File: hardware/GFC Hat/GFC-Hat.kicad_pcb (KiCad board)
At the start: 2 copper layers, 65 x 30 mm, 36 parts, among them J1 BAT, U2 CAT24C32WI-GT3, U3 BME280

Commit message: Started making some revisions to Prototype 2, cleaned up files.
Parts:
- removed I2C3: I2C0, Connector_PinHeader_2.00mm:PinHeader_1x04_P2.00mm_Vertical
- removed LED1: Status LED, LED_SMD:LED_0805_2012Metric
- removed R2: R, Resistor_SMD:R_0603_1608Metric_Pad0.98x0.95mm_HandSolder
- removed TMP1, TMP2, TMP3: 1-Wire Bus, Connector_PinHeader_2.00mm:PinHeader_1x03_P2.00mm_Vertical
- removed TP1: Test Point, TestPoint:TestPoint_Pad_D1.0mm
- removed the U2 at (62.5, 62.0)
- added 1W1: 1-Wire Bus, GFC-Hat-Footprints:JST_PH_B3B-PH-K_1x03_P2.00mm_Vertical, F.Cu at (78.2, 35.5)
- added 1W2: 1-Wire Bus, GFC-Hat-Footprints:JST_PH_B3B-PH-K_1x03_P2.00mm_Vertical, F.Cu at (78.2, 41.0)
- added C12: 0.1uF, Capacitor_SMD:C_0603_1608Metric_Pad1.08x0.95mm_HandSolder, F.Cu at (170.4, 5.73)
- added C13: 0.1uF, Capacitor_SMD:C_0603_1608Metric_Pad1.08x0.95mm_HandSolder, F.Cu at (183.4, 6.10)
- added C14: 0.1uF, Capacitor_SMD:C_0603_1608Metric_Pad1.08x0.95mm_HandSolder, F.Cu at (203.5, -13.9)
- added C18: 0.1uF, Capacitor_SMD:C_0603_1608Metric_Pad1.08x0.95mm_HandSolder, F.Cu at (107.6, 24.6)
- added U1: MAX17048G+T10, MAX17048G_T10:SON50P200X200X80-9N, F.Cu at (34.2, 42.1)
- added U3: CAT24C32WI-GT3, footprints:SOIC127P600X175-8N, B.Cu at (81.5, 26.4)
- added U4: DS18B20, Package_TO_SOT_THT:TO-92_Inline, F.Cu at (76.0, 30.7)
- C1: renamed from C2; footprint Capacitor_THT:CP_Radial_D6.3mm_P2.50mm -> Capacitor_SMD:C_Elec_6.3x7.7
- C2: renamed from C3; footprint Capacitor_SMD:C_0603_1608Metric_Pad1.08x0.95mm_HandSolder -> Capacitor_SMD:C_0805_2012Metric_Pad1.18x1.45mm_HandSolder
- C6: value 100nF -> 0.1uF
- D1: value 1N5400 -> 2A LFV; footprint Diode_THT:D_DO-15_P12.70mm_Horizontal -> Diode_SMD:D_SMA_Handsoldering
- I2C1, I2C2: footprint Connector_PinHeader_2.00mm:PinHeader_1x04_P2.00mm_Vertical -> GFC-Hat-Footprints:JST_PH_B4B-PH-K_1x04_P2.00mm_Vertical
- J1: footprint Library:OSTVN02A150 2x1 Terminal Block -> GFC-Hat-Footprints:OSTVN02A150 2x1 Terminal Block
- PI_HDR1: renamed from CPU1; value Pi Zero/Zero W -> PI Header
- SPI1, SPI2: footprint Connector_PinHeader_2.00mm:PinHeader_1x06_P2.00mm_Vertical -> GFC-Hat-Footprints:JST_PH_B6B-PH-K_1x06_P2.00mm_Vertical
- moved PR2 136.5 mm to (174.7, 8.24)
- moved C3 131.5 mm to (21.5, 38.3), turned to -90 degrees
- moved PR1 128.3 mm to (170.4, 8.24), turned to 0 degrees
- moved C9 125.5 mm to (31.1, 31.9)
- moved C5 125.0 mm to (35.4, 39.8)
- moved C7 122.6 mm to (31.1, 33.5)
- moved C2 116.5 mm to (23.6, 36.0), turned to 90 degrees
- moved C1 89.6 mm to (28.4, 39.0)
- moved R1 68.8 mm to (74.0, 38.0)
- moved U2 66.0 mm to (31.4, 29.4)
- moved G*** 40.7 mm to (113.0, 79.0)
- moved C6 39.0 mm to (174.7, 5.73)
- moved C10 34.9 mm to (179.1, 5.73)
- moved SPI1 32.9 mm to (48.5, 28.8), turned to 0 degrees
- moved SPI2 30.4 mm to (48.5, 34.7), turned to 0 degrees
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- renumbered C12 to C15, C13 to C16, C4 to C3, C5 to C4, C1 to C5, U3 to U2
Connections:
- C10 pad 1: +3V3 -> GND
- PI_HDR1 pad 16: /Status LED GPIO -> unconnected-(PI_HDR1-Pad16)
- R3 pad 2: +3V3 -> GND
- R4 pad 2: +3V3 -> GND
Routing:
- net +3V3: track 68.6 -> 0.00 mm
- net I2C0.SDA: track 29.8 -> 0.00 mm
- net I2C0.SCL: track 27.1 -> 0.00 mm
- net EEPROM.SDA: track 0.00 -> 23.7 mm
- net EEPROM.SCL: track 0.00 -> 23.6 mm
- net GND: track 17.9 -> 0.00 mm, vias 2 -> 0
- net 1-Wire: track 15.5 -> 0.00 mm
- net SPI0.MOSI: track 14.6 -> 0.00 mm
- net /VCC Polarized: track 0.00 -> 13.7 mm, vias 0 -> 2
- net SPI0.MISO: track 11.5 -> 0.00 mm
- net SPI0.SCLK: track 10.1 -> 0.00 mm
- net SPI0.CE0: track 8.82 -> 0.00 mm
- net SPI0.CE1: track 7.60 -> 0.00 mm
- net VCC: track 0.00 -> 3.93 mm
- net +5V: track 21.3 -> 18.2 mm
- removed copper zone on B.Cu, net GND
- removed copper zone on F.Cu, net GND
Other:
- outline, holes or cut-outs redrawn
- board text added: "GFC PROTOTYPE 2"
- board text removed: "GFC PROTOTYPE 1"
- board text removed: "HAT"

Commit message: GFC Prototype 2 Complete and ordered - with BOM
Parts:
- removed C16: 0.1uF, Capacitor_SMD:C_0603_1608Metric_Pad1.08x0.95mm_HandSolder
- removed the G*** at (113.0, 79.0)
- removed I2C2: I2C0, GFC-Hat-Footprints:JST_PH_B4B-PH-K_1x04_P2.00mm_Vertical
- removed SPI1, SPI2: SPI, GFC-Hat-Footprints:JST_PH_B6B-PH-K_1x06_P2.00mm_Vertical
- added C17: 0.1µF, Capacitor_SMD:C_0603_1608Metric, B.Cu at (29.7, 38.8)
- added C19: 0.1µF, Capacitor_SMD:C_0603_1608Metric, F.Cu at (68.8, 29.1)
- added G***: LOGO, footprints:logo2, F.Cu at (59.1, 43.1)
- added R2: 30kΩ, Resistor_SMD:R_0603_1608Metric, B.Cu at (29.4, 35.5)
- added R5: 7.5kΩ, Resistor_SMD:R_0603_1608Metric, B.Cu at (32.2, 38.3)
- added TP1: GND REF, TestPoint:TestPoint_Keystone_5019_Minature, B.Cu at (22.5, 42.6)
- added TP2: BAT REF, TestPoint:TestPoint_Pad_D1.5mm, F.Cu at (33.0, 40.8)
- added U5: BMI088, GFC-Footprints:PQFN50P450X300X100-16N, B.Cu at (52.5, 35.0)
- 1W1, 1W2: value 1-Wire Bus -> 1-Wire; footprint GFC-Hat-Footprints:JST_PH_B3B-PH-K_1x03_P2.00mm_Vertical -> Connector_PinHeader_1.27mm:PinHeader_1x03_P1.27mm_Vertical
- C1: value 100uF -> 100µF; moved to B.Cu
- C10, C11, C12, C14, C18, C7, C9: value 0.1uF -> 0.1µF; footprint Capacitor_SMD:C_0603_1608Metric_Pad1.08x0.95mm_HandSolder -> Capacitor_SMD:C_0603_1608Metric
- C13, C15, C3, C4, C5, C6, C8: value 0.1uF -> 0.1µF; footprint Capacitor_SMD:C_0603_1608Metric_Pad1.08x0.95mm_HandSolder -> Capacitor_SMD:C_0603_1608Metric; moved to B.Cu
- C2: value 1uF -> 1µF; footprint Capacitor_SMD:C_0805_2012Metric_Pad1.18x1.45mm_HandSolder -> Capacitor_SMD:C_0805_2012Metric; moved to B.Cu
- D1: footprint Diode_SMD:D_SMA_Handsoldering -> Diode_SMD:D_SMA
- I2C1: value I2C0 -> I²C; footprint GFC-Hat-Footprints:JST_PH_B4B-PH-K_1x04_P2.00mm_Vertical -> Connector_PinHeader_1.27mm:PinHeader_1x04_P1.27mm_Vertical
- J1: footprint GFC-Hat-Footprints:OSTVN02A150 2x1 Terminal Block -> GFC-Footprints:OSTVN02A150 2x1 Terminal Block
- PI_HDR1: value PI Header -> PI
- PR1, PR2: value * -> Pull-up
- R1: value 4.7k -> 4.7kΩ; footprint Resistor_SMD:R_0603_1608Metric_Pad0.98x0.95mm_HandSolder -> Resistor_SMD:R_0603_1608Metric
- R3, R4: value 3.9K -> 3.9kΩ; footprint Resistor_SMD:R_0603_1608Metric_Pad0.98x0.95mm_HandSolder -> Resistor_SMD:R_0603_1608Metric
- U1: value MAX17048G+T10 -> MCP3021; footprint MAX17048G_T10:SON50P200X200X80-9N -> Package_TO_SOT_SMD:SOT-23-5; moved to B.Cu
- U3: value CAT24C32WI-GT3 -> CAT24C32
- U4: value DS18B20 -> SAM-M8Q; footprint Package_TO_SOT_THT:TO-92_Inline -> RF_GPS:ublox_SAM-M8Q
- VR1: moved to F.Cu
- moved C14 177.7 mm to (36.0, 45.7)
- moved C6 150.5 mm to (25.1, 21.5), turned to 180 degrees
- moved C12 146.3 mm to (29.7, 45.7)
- moved PR2 141.7 mm to (37.0, 41.6), turned to -90 degrees
- moved C13 137.4 mm to (49.0, 34.5)
- moved PR1 136.0 mm to (38.5, 41.6), turned to -90 degrees
- moved C4 120.3 mm to (25.6, 27.4), turned to -90 degrees
- moved C10 109.3 mm to (72.3, 29.1), turned to 180 degrees
- moved C11 105.9 mm to (40.8, 45.7)
- moved C15 97.6 mm to (55.3, 36.3), turned to 90 degrees
- moved R4 69.6 mm to (79.4, 24.6), turned to -90 degrees
- moved C8 62.8 mm to (82.5, 21.5)
- moved R3 61.9 mm to (81.0, 24.6), turned to -90 degrees
- moved 1W1 51.9 mm to (27.9, 48.2), turned to 90 degrees
- moved 1W2 44.6 mm to (34.2, 48.2), turned to 90 degrees
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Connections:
- net /VCC Polarized renamed BAT_P
- C10 pad 2: GND -> +3V3
- C18 pad 1: +3V3 -> GND
- C18 pad 2: GND -> +3V3
- C5 pad 1: VCC -> GND
- C5 pad 2: GND -> +3V3
- D1 pad 2: VCC -> +BATT
- I2C1 pad 2: I2C0.SCL -> +3V3
- I2C1 pad 4: +3V3 -> I2C0.SCL
- J1 pad 1: VCC -> +BATT
- PI_HDR1 pad 13: unconnected-(PI_HDR1-Pad13) -> BMI088 Int1
- PI_HDR1 pad 15: unconnected-(PI_HDR1-Pad15) -> BMI088 Int3
- PI_HDR1 pad 37: unconnected-(PI_HDR1-Pad37) -> TX_Ready GPIO
- R3 pad 2: GND -> +3V3
- R4 pad 2: GND -> +3V3
- U1 pad 1: GND -> +3V3
- U1 pad 2: VCC -> GND
- U1 pad 3: +3V3 -> /BAT Reference
- U1 pad 4: GND -> I2C0.SDA
- U1 pad 5: unconnected-(U1-Pad5) -> I2C0.SCL
- U4 pad 2: 1-Wire -> +3V3
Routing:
- net I2C0.SDA: track 0.00 -> 71.0 mm, vias 0 -> 3
- net I2C0.SCL: track 0.00 -> 67.6 mm, vias 0 -> 2
- net GND: track 0.00 -> 48.1 mm, vias 0 -> 59
- net +3V3: track 0.00 -> 46.9 mm, vias 0 -> 19
- net TX_Ready GPIO: track 0.00 -> 41.8 mm, vias 0 -> 1
- net 1-Wire: track 0.00 -> 38.8 mm, vias 0 -> 1
- net BMI088 Int1: track 0.00 -> 21.4 mm
- net SPI0.CE0: track 0.00 -> 18.0 mm
- net SPI0.CE1: track 0.00 -> 17.0 mm
- net BMI088 Int3: track 0.00 -> 16.2 mm, vias 0 -> 2
- net SPI0.MISO: track 0.00 -> 14.7 mm, vias 0 -> 2
- net SPI0.SCLK: track 0.00 -> 11.1 mm
- net /BAT Reference: track 0.00 -> 10.5 mm, vias 0 -> 1
- net SPI0.MOSI: track 0.00 -> 8.73 mm
- net VCC: track 3.93 -> 0.00 mm
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- added copper zone on In2.Cu, net +3V3
- added copper zone on B.Cu, net GND
- added copper zone on F.Cu, net GND
- added copper zone on In1.Cu, net GND
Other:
- outline, holes or cut-outs redrawn
- copper layers 2 -> 4
- board text added: "IMU"

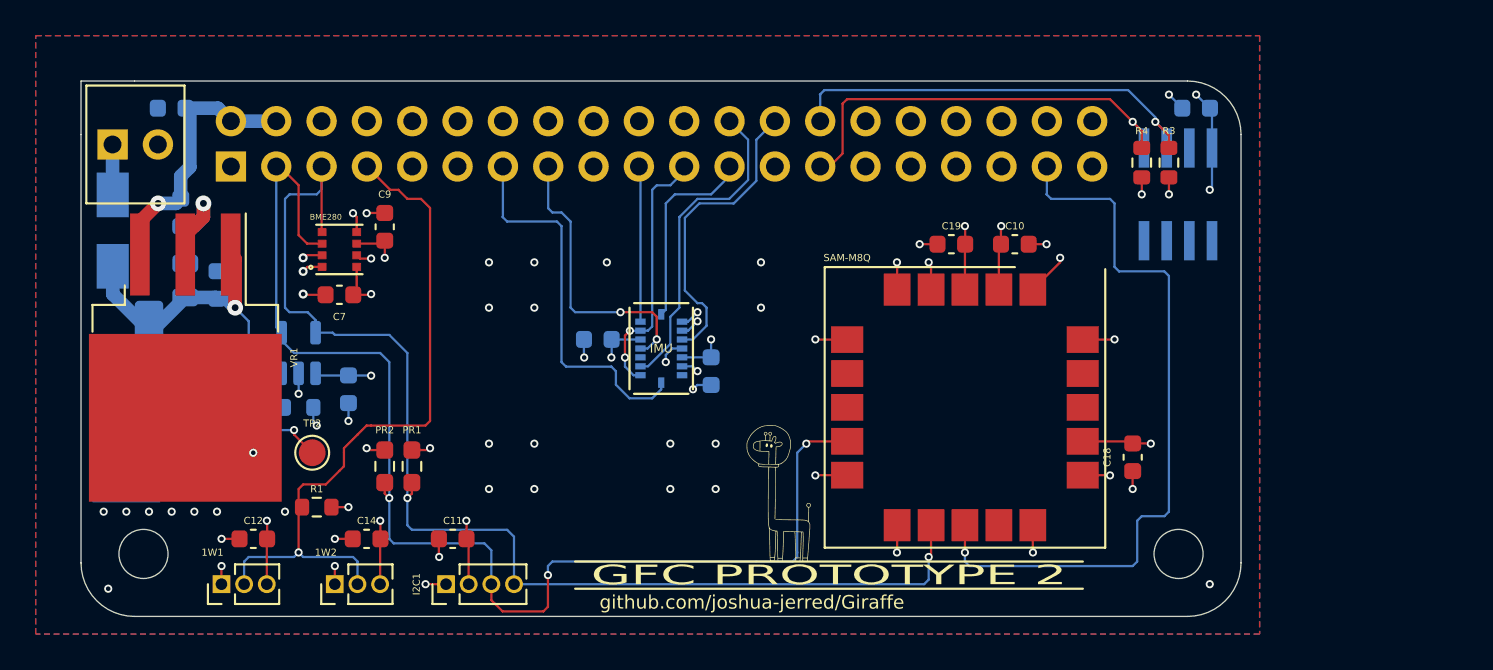
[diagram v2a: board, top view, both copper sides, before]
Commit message: Hardware update to bring it up to KiCad 7.0
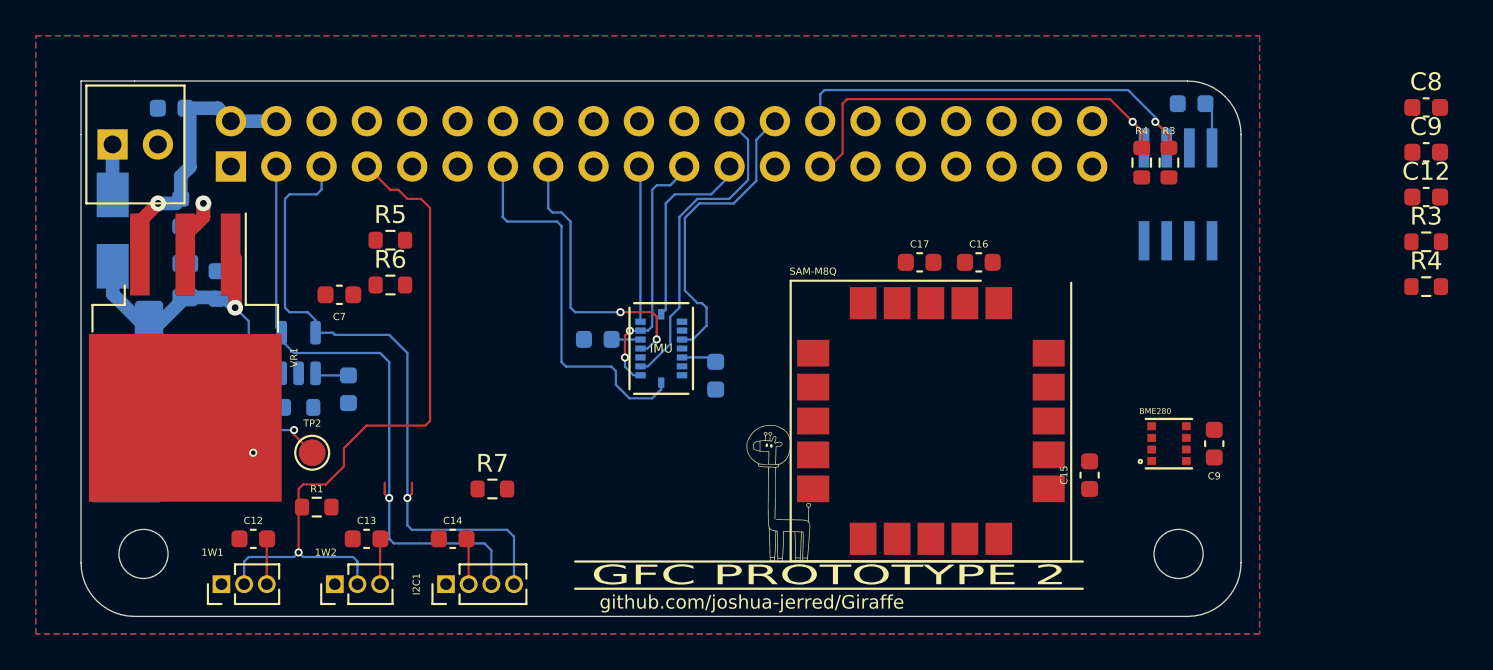
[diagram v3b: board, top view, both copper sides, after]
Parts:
- removed PR1, PR2: Pull-up, Resistor_SMD:R_0603_1608Metric_Pad0.98x0.95mm_HandSolder
- added C12: 0.1µF, Capacitor_SMD:C_0603_1608Metric, F.Cu at (95.4, 26.5)
- added C8: 0.1µF, Capacitor_SMD:C_0603_1608Metric, F.Cu at (95.4, 21.5)
- added C9: 0.1µF, Capacitor_SMD:C_0603_1608Metric, F.Cu at (95.4, 24.0)
- added R3: 3.9kΩ, Resistor_SMD:R_0603_1608Metric, F.Cu at (95.4, 29.0)
- added R4: 3.9kΩ, Resistor_SMD:R_0603_1608Metric, F.Cu at (95.4, 31.5)
- added R5: *, Resistor_SMD:R_0603_1608Metric, F.Cu at (37.3, 28.9)
- added R6: *, Resistor_SMD:R_0603_1608Metric, F.Cu at (37.3, 31.4)
- added R7: 4.7kΩ, Resistor_SMD:R_0603_1608Metric, F.Cu at (43.0, 42.9)
- R1: value 4.7kΩ -> 30kΩ
- U3: footprint footprints:SOIC127P600X175-8N -> GFC-Footprints:SOIC127P600X175-8N
- moved C9 48.0 mm to (83.5, 40.3), turned to -90 degrees
- moved U2 47.7 mm to (81.0, 40.3)
- moved C15 2.61 mm to (76.5, 42.1)
- moved C16 2.26 mm to (70.3, 30.2)
- moved U4 2.05 mm to (67.6, 39.0)
- moved C17 2.05 mm to (67.0, 30.2)
- moved C18 0.36 mm to (55.6, 36.5)
- moved C10 0.36 mm to (82.2, 21.3)
- renumbered C8 to C10, C13 to C11, C14 to C13, C11 to C14, C18 to C15, C10 to C16, C19 to C17, C15 to C18, C6 to C5, C5 to C6, C17 to C7, R2 to R1, R5 to R2
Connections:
- net TX_Ready GPIO renamed GPS TX-Ready
- C1 pad 1: BAT_P -> BAT Polarized
- C14 pad 1: GND -> +3V3
- C14 pad 2: +3V3 -> GND
- C2 pad 1: BAT_P -> BAT Polarized
- C3 pad 1: BAT_P -> BAT Polarized
- C5 pad 1: +5V -> GND
- C5 pad 2: GND -> +5V
- C7 pad 2: +3V3 -> /BAT Reference Voltage
- C7 pad 2: /BAT Reference -> /BAT Reference Voltage
- C9 pad 1: +3V3 -> GND
- C9 pad 2: GND -> +3V3
- D1 pad 1: BAT_P -> BAT Polarized
- I2C1 pad 3: I2C0.SDA -> I2C0.SCL
- I2C1 pad 4: I2C0.SCL -> I2C0.SDA
- PI_HDR1 pad 13: BMI088 Int1 -> unconnected-(PI_HDR1-GPIO27-Pad13)
- PI_HDR1 pad 33: unconnected-(PI_HDR1-Pad33) -> BMI088 Int1
- R1 pad 1: 1-Wire -> BAT Polarized
- R1 pad 2: +3V3 -> /BAT Reference Voltage
- R1 pad 1: BAT_P -> BAT Polarized
- R1 pad 2: /BAT Reference -> /BAT Reference Voltage
- R2 pad 1: /BAT Reference -> /BAT Reference Voltage
- R3 pad 1: EEPROM.SCL -> +3V3
- R3 pad 2: +3V3 -> EEPROM.SDA
- R4 pad 1: EEPROM.SDA -> +3V3
- R4 pad 2: +3V3 -> EEPROM.SCL
- TP2 pad 1: /BAT Reference -> /BAT Reference Voltage
- U1 pad 3: /BAT Reference -> /BAT Reference Voltage
- VR1 pad 1: BAT_P -> BAT Polarized
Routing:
- net GPS TX-Ready: track 41.8 -> 0.00 mm, vias 1 -> 0
- net GND: track 48.1 -> 6.79 mm, vias 59 -> 2
- net I2C0.SDA: track 71.0 -> 35.2 mm, vias 3 -> 1
- net +3V3: track 46.9 -> 15.1 mm, vias 19 -> 0
- net I2C0.SCL: track 67.6 -> 37.5 mm, vias 2 -> 1
- net BAT_P: track 15.6 -> 0.00 mm, vias 1 -> 0
- net BAT Polarized: track 0.00 -> 15.6 mm, vias 0 -> 1
- net /BAT Reference Voltage: track 0.00 -> 10.5 mm, vias 0 -> 1
- net /BAT Reference: track 10.5 -> 0.00 mm, vias 1 -> 0

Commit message: booster seat update with file system functions
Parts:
- removed the C9 at (95.4, 24.0)
- moved R3 53.0 mm to (42.4, 30.8)
- moved R4 53.0 mm to (42.4, 33.3)
- moved C12 49.9 mm to (48.7, 44.1)
- moved C8 26.4 mm to (80.8, 43.5)
- moved C16 2.05 mm to (68.3, 30.2)
- moved C17 1.91 mm to (65.1, 30.2)
- moved U4 1.91 mm to (65.7, 39.0)
